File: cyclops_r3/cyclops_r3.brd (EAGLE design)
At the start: 124.5 x 79.9 mm, 107 parts, among them Q1 BC817, Q2 IRF510, U1 MCP4921, U2 MCP4022-50k, U3 317-N, U4 TLV3701, U5 337-N, U6 ADR03, U7 OP1177, U8 LTC2052HV, U9 ZXTD45

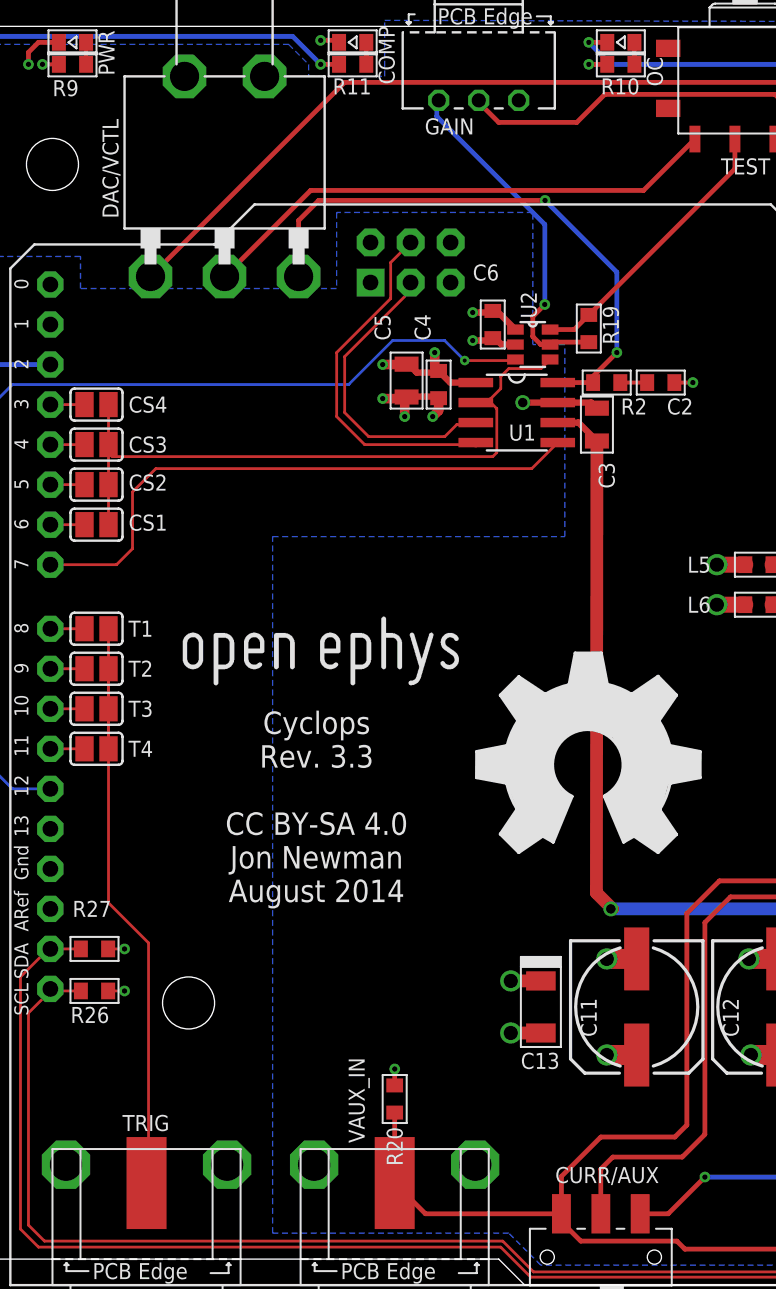
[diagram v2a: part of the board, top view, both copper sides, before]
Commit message: Assembed r3.3 and started a TODO list. Started driver code.
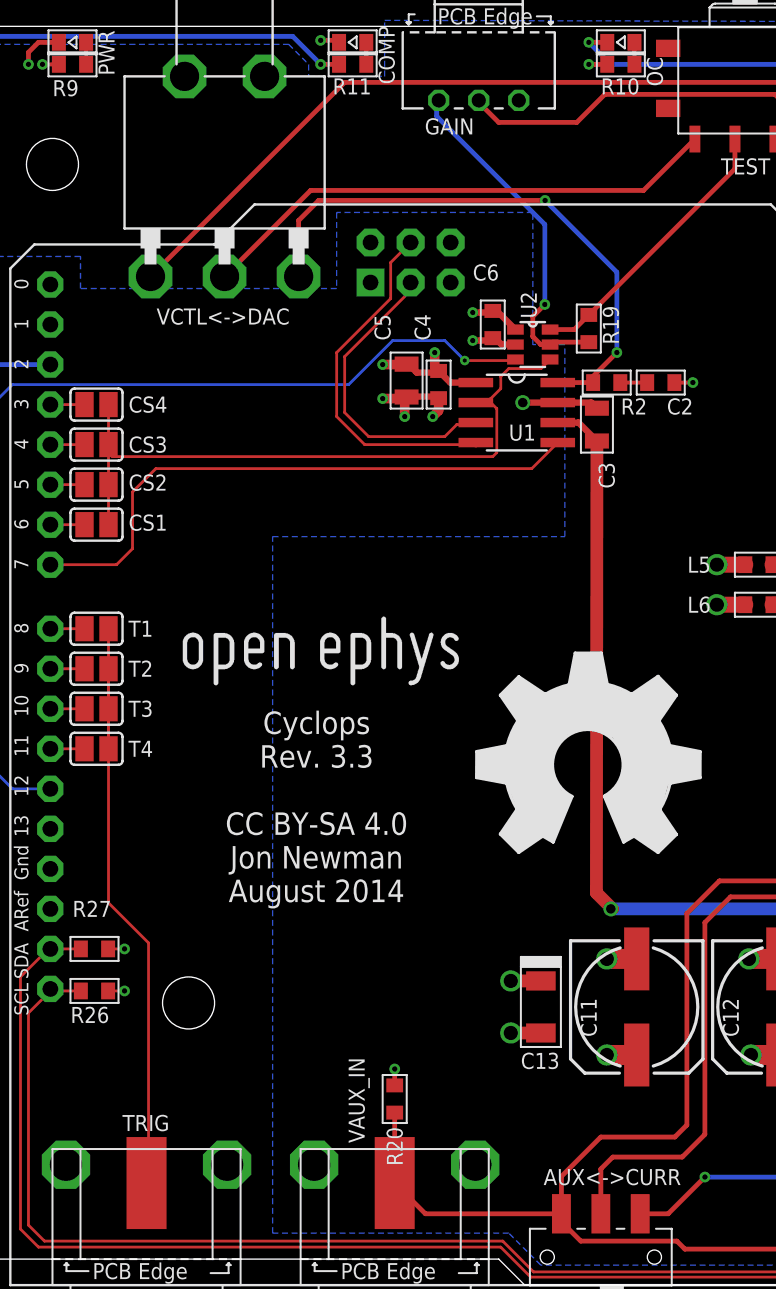
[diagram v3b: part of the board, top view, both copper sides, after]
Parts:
- renumbered CURR/AUX to AUX<->CURR, DAC/VCTL to VCTL<->DAC
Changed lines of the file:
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@@
 <?xml version="1.0" encoding="utf-8"?>
 <!DOCTYPE eagle SYSTEM "eagle.dtd">
-<eagle version="6.5.0">
+<eagle version="6.6.0">
 <drawing>
 <settings>
@@
 <attribute name="VALUE" x="68.714" y="52.705" size="1.016" layer="27" font="vector" ratio="18"/>
 </element>
-<element name="CURR/AUX" library="cyclops" package="JS102011SAQN" value="JS102" x="41.656" y="1.778" smashed="yes">
-<attribute name="NAME" x="45.353" y="7.493" size="1.016" layer="25" font="vector" ratio="18" rot="R180"/>
+<element name="AUX&lt;-&gt;CURR" library="cyclops" package="JS102011SAQN" value="JS102" x="41.656" y="1.778" smashed="yes">
+<attribute name="NAME" x="46.75" y="7.366" size="1.016" layer="25" font="vector" ratio="18" rot="R180"/>
 <attribute name="VALUE" x="43.956" y="2.286" size="1.016" layer="27" font="vector" ratio="18" rot="R180"/>
 </element>
@@
 <attribute name="VALUE" x="35.306" y="73.025" size="1.016" layer="27" font="vector" ratio="18"/>
 </element>
-<element name="DAC/VCTL" library="cyclops" package="2M1-SP1-T2-B4-M6RE" value="2M1" x="17.78" y="76.2" smashed="yes" rot="R270">
-<attribute name="NAME" x="11.049" y="67.691" size="1.016" layer="25" font="vector" ratio="18" rot="R90"/>
+<element name="VCTL&lt;-&gt;DAC" library="cyclops" package="2M1-SP1-T2-B4-M6RE" value="2M1" x="17.78" y="76.2" smashed="yes" rot="R270">
+<attribute name="NAME" x="13.462" y="60.96" size="1.016" layer="25" font="vector" ratio="18"/>
 <attribute name="VALUE" x="16.383" y="73.914" size="1.016" layer="27" font="vector" ratio="18"/>
 </element>
@@
 <signal name="VFB">
 <contactref element="U8" pad="6"/>
-<contactref element="CURR/AUX" pad="2"/>
+<contactref element="AUX&lt;-&gt;CURR" pad="2"/>
 <wire x1="65.084" y1="40.64" x2="60.325" y2="40.64" width="0.3048" layer="1"/>
 <wire x1="60.325" y1="40.64" x2="58.801" y2="39.116" width="0.3048" layer="1"/>
@@
 <contactref element="U1" pad="8"/>
 <contactref element="R2" pad="2"/>
-<contactref element="DAC/VCTL" pad="1"/>
+<contactref element="VCTL&lt;-&gt;DAC" pad="1"/>
 <wire x1="38.1184" y1="68.834" x2="23.749" y2="68.834" width="0.3048" layer="1"/>
 <wire x1="23.749" y1="68.834" x2="22.479" y2="67.564" width="0.3048" layer="1"/>
@@
 <wire x1="60.706" y1="44.069" x2="64.703" y2="44.069" width="0.3048" layer="1"/>
 <wire x1="64.703" y1="44.069" x2="65.084" y2="44.45" width="0.3048" layer="1"/>
-<contactref element="CURR/AUX" pad="1"/>
+<contactref element="AUX&lt;-&gt;CURR" pad="1"/>
 <wire x1="28.575" y1="6.477" x2="30.524" y2="4.528" width="0.3048" layer="1"/>
 <wire x1="30.524" y1="4.528" x2="39.156" y2="4.528" width="0.3048" layer="1"/>
@@
 <signal name="N$34">
 <contactref element="TEST" pad="3"/>
-<contactref element="DAC/VCTL" pad="2"/>
+<contactref element="VCTL&lt;-&gt;DAC" pad="2"/>
 <wire x1="17.78" y1="64.008" x2="23.241" y2="69.469" width="0.3048" layer="1"/>
 <wire x1="23.241" y1="69.469" x2="44.365" y2="69.469" width="0.3048" layer="1"/>
@@
 <signal name="VINPUT">
 <contactref element="VCTL" pad="1"/>
-<contactref element="DAC/VCTL" pad="3"/>
+<contactref element="VCTL&lt;-&gt;DAC" pad="3"/>
 <wire x1="25.4" y1="76.327" x2="65.405" y2="76.327" width="0.3048" layer="1"/>
 <wire x1="65.405" y1="76.327" x2="68.326" y2="73.406" width="0.3048" layer="1"/>
@@
 <wire x1="85.979" y1="8.763" x2="86.487" y2="8.763" width="1.4224" layer="1"/>
 <wire x1="86.487" y1="8.763" x2="87.249" y2="9.525" width="1.4224" layer="1"/>
-<contactref element="CURR/AUX" pad="3"/>
+<contactref element="AUX&lt;-&gt;CURR" pad="3"/>
 <wire x1="44.327" y1="4.699" x2="44.156" y2="4.528" width="0.8128" layer="1" curve="90"/>
 <wire x1="120.269" y1="22.352" x2="120.269" y2="44.323" width="3.048" layer="1"/>

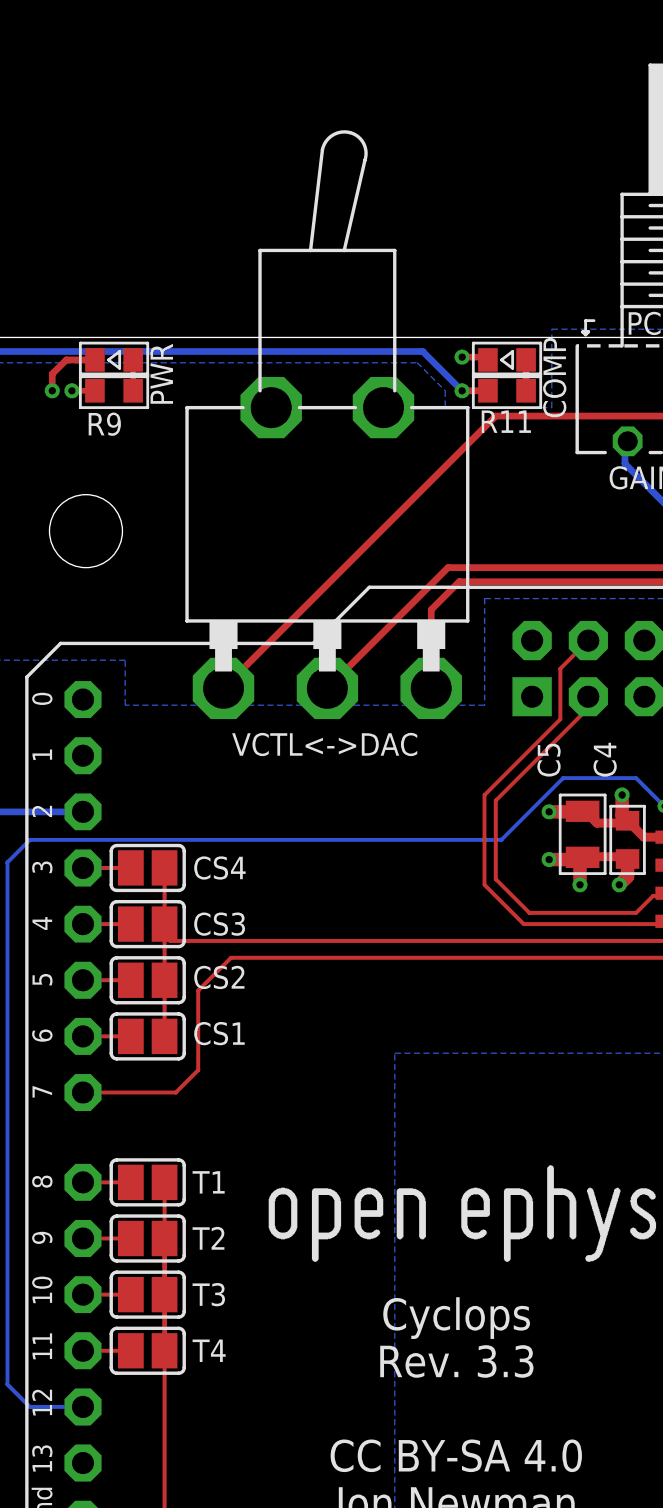
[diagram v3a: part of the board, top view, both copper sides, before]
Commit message: Asthetic fixes to board. Driver has limited functionality and is pretty inefficient, but the base stuff is there.
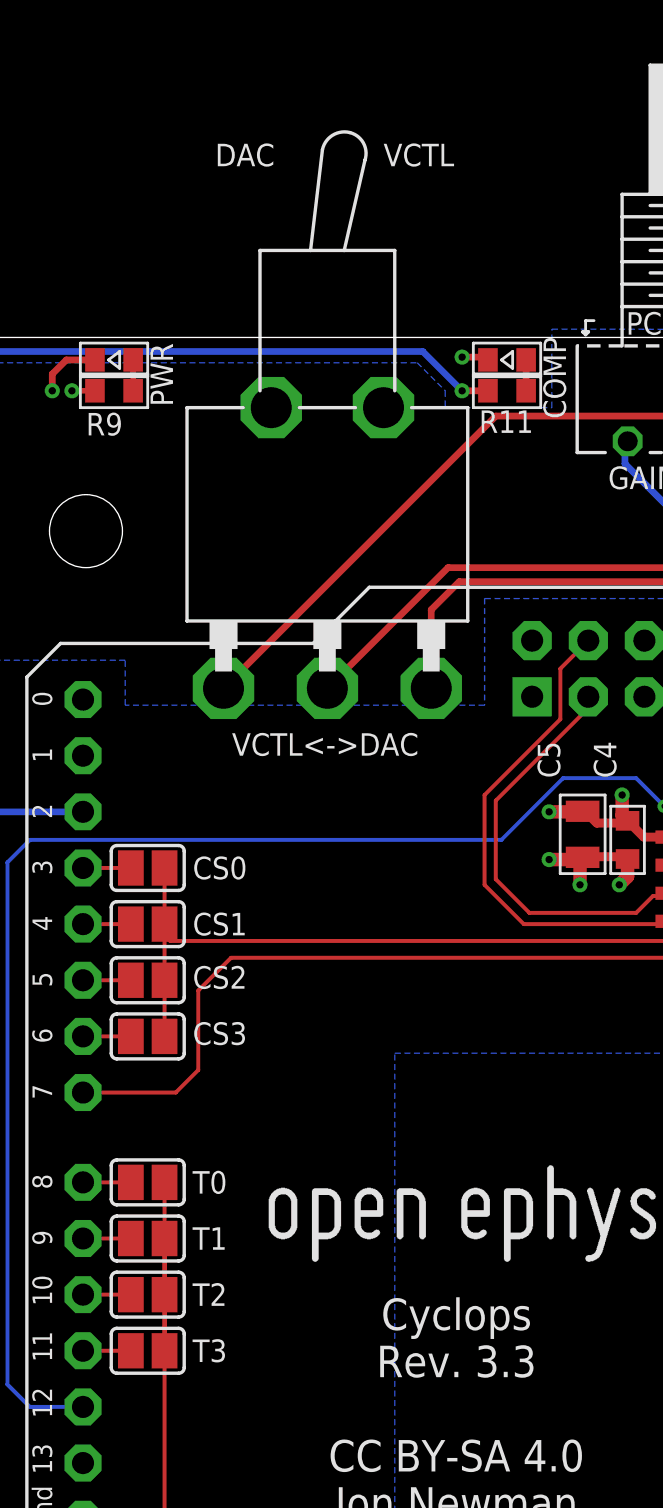
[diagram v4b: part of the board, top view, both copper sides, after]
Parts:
- removed T4: (no value), cyclops:SJ
- added T0: (no value), cyclops:SJ
- moved CS1 5.08 mm to (9.65, 53.3)
- moved CS3 5.08 mm to (9.65, 48.3)
- moved T1 2.54 mm to (9.65, 39.1)
- moved T2 2.54 mm to (9.65, 36.6)
- moved T3 2.54 mm to (9.65, 34.0)
- renumbered CS4 to CS0
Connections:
- net CS1: now also CS1.1; no longer CS3.1
- net CS3: now also CS3.1; no longer CS1.1
- net T0: now also T0.2; no longer T1.2
- net T1: now also T1.2; no longer T2.2
- net T2: now also T2.2; no longer T3.2
- net T3: now also T3.2; no longer T4.2
- net TRIG: now also T0.1; no longer T4.1
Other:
- board text added: "DAC"
- board text added: "VCTL"
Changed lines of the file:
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@@
 <setting verticaltext="up"/>
 </settings>
-<grid distance="0.005" unitdist="inch" unit="inch" style="lines" multiple="1" display="yes" altdistance="0.025" altunitdist="inch" altunit="inch"/>
+<grid distance="0.05" unitdist="inch" unit="inch" style="lines" multiple="1" display="yes" altdistance="0.025" altunitdist="inch" altunit="inch"/>
 <layers>
 <layer number="1" name="Top" color="4" fill="1" visible="yes" active="yes"/>
@@
 <text x="69.215" y="9.525" size="1.016" layer="21" font="vector" ratio="18" rot="R90" align="center">-6V</text>
 <text x="61.595" y="13.97" size="1.016" layer="21" font="vector" ratio="18" align="center">GND</text>
+<text x="20.32" y="87.63" size="1.016" layer="21" font="vector" ratio="18">VCTL</text>
+<text x="12.7" y="87.63" size="1.016" layer="21" font="vector" ratio="18">DAC</text>
 </plain>
 <attributes>
@@
 <attribute name="VALUE" x="72.263" y="45.72" size="1.016" layer="27" font="vector" ratio="18" rot="R90" align="center-left"/>
 </element>
-<element name="CS1" library="cyclops" package="SJ" value="" x="9.652" y="48.26" smashed="yes">
+<element name="CS3" library="cyclops" package="SJ" value="" x="9.652" y="48.26" smashed="yes">
 <attribute name="NAME" x="11.684" y="47.879" size="1.016" layer="25" font="vector" ratio="18"/>
 <attribute name="VALUE" x="10.0521" y="48.26" size="0.02" layer="27"/>
@@
 <attribute name="VALUE" x="10.0521" y="50.8" size="0.02" layer="27"/>
 </element>
-<element name="CS3" library="cyclops" package="SJ" value="" x="9.652" y="53.34" smashed="yes">
+<element name="CS1" library="cyclops" package="SJ" value="" x="9.652" y="53.34" smashed="yes">
 <attribute name="NAME" x="11.684" y="52.832" size="1.016" layer="25" font="vector" ratio="18"/>
 <attribute name="VALUE" x="10.0521" y="53.34" size="0.02" layer="27"/>
 </element>
-<element name="CS4" library="cyclops" package="SJ" value="" x="9.652" y="55.88" smashed="yes">
+<element name="CS0" library="cyclops" package="SJ" value="" x="9.652" y="55.88" smashed="yes">
 <attribute name="NAME" x="11.684" y="55.372" size="1.016" layer="25" font="vector" ratio="18"/>
 <attribute name="VALUE" x="10.0521" y="55.88" size="0.02" layer="27"/>
@@
 <attribute name="VALUE" x="28.575" y="13.589" size="1.016" layer="27" font="vector" ratio="18" rot="R90" align="center-left"/>
 </element>
-<element name="T1" library="cyclops" package="SJ" value="" x="9.652" y="41.656" smashed="yes" rot="R180">
+<element name="T0" library="cyclops" package="SJ" value="" x="9.652" y="41.656" smashed="yes" rot="R180">
 <attribute name="NAME" x="11.684" y="41.148" size="1.016" layer="25" font="vector" ratio="18"/>
 <attribute name="VALUE" x="9.2519" y="41.656" size="0.02" layer="27" rot="R180"/>
 </element>
-<element name="T2" library="cyclops" package="SJ" value="" x="9.652" y="39.116" smashed="yes" rot="R180">
+<element name="T1" library="cyclops" package="SJ" value="" x="9.652" y="39.116" smashed="yes" rot="R180">
 <attribute name="NAME" x="11.684" y="38.608" size="1.016" layer="25" font="vector" ratio="18"/>
 <attribute name="VALUE" x="9.2519" y="39.116" size="0.02" layer="27" rot="R180"/>
 </element>
-<element name="T3" library="cyclops" package="SJ" value="" x="9.652" y="36.576" smashed="yes" rot="R180">
+<element name="T2" library="cyclops" package="SJ" value="" x="9.652" y="36.576" smashed="yes" rot="R180">
 <attribute name="NAME" x="11.684" y="36.068" size="1.016" layer="25" font="vector" ratio="18"/>
 <attribute name="VALUE" x="9.2519" y="36.576" size="0.02" layer="27" rot="R180"/>
 </element>
-<element name="T4" library="cyclops" package="SJ" value="" x="9.652" y="34.036" smashed="yes" rot="R180">
+<element name="T3" library="cyclops" package="SJ" value="" x="9.652" y="34.036" smashed="yes" rot="R180">
 <attribute name="NAME" x="11.684" y="33.528" size="1.016" layer="25" font="vector" ratio="18"/>
 <attribute name="VALUE" x="9.2519" y="34.036" size="0.02" layer="27" rot="R180"/>
@@
 </signal>
 <signal name="CS0">
-<contactref element="CS4" pad="1"/>
+<contactref element="CS0" pad="1"/>
 <contactref element="LEONARDO" pad="D3"/>
 <wire x1="8.89" y1="55.88" x2="6.724" y2="55.88" width="0.1778" layer="1"/>
 </signal>
 <signal name="CS1">
-<contactref element="CS3" pad="1"/>
+<contactref element="CS1" pad="1"/>
 <contactref element="LEONARDO" pad="D4"/>
 <wire x1="6.724" y1="53.34" x2="8.89" y2="53.34" width="0.1778" layer="1"/>
 </signal>
 <signal name="CS3">
-<contactref element="CS1" pad="1"/>
+<contactref element="CS3" pad="1"/>
 <contactref element="LEONARDO" pad="D6"/>
 <wire x1="6.724" y1="48.26" x2="8.89" y2="48.26" width="0.1778" layer="1"/>
@@
 <signal name="CS">
 <contactref element="U1" pad="2"/>
-<contactref element="CS4" pad="2"/>
+<contactref element="CS0" pad="2"/>
+<contactref element="CS1" pad="2"/>
+<contactref element="CS2" pad="2"/>
 <contactref element="CS3" pad="2"/>
-<contactref element="CS2" pad="2"/>
-<contactref element="CS1" pad="2"/>
 <wire x1="10.414" y1="55.88" x2="10.414" y2="53.34" width="0.1778" layer="1"/>
 <wire x1="10.414" y1="52.832" x2="10.414" y2="53.34" width="0.1778" layer="1"/>
@@
 </signal>
 <signal name="TRIG">
+<contactref element="T0" pad="1"/>
 <contactref element="T1" pad="1"/>
 <contactref element="T2" pad="1"/>
 <contactref element="T3" pad="1"/>
-<contactref element="T4" pad="1"/>
 <contactref element="TRIG" pad="1"/>
 <wire x1="12.827" y1="6.477" x2="12.827" y2="9.144" width="0.1778" layer="1"/>
@@
 </signal>
 <signal name="T0">
-<contactref element="T1" pad="2"/>
+<contactref element="T0" pad="2"/>
 <contactref element="LEONARDO" pad="D8"/>
 <wire x1="8.89" y1="41.656" x2="6.724" y2="41.656" width="0.1778" layer="1"/>
 </signal>
 <signal name="T1">
-<contactref element="T2" pad="2"/>
+<contactref element="T1" pad="2"/>
 <contactref element="LEONARDO" pad="D9"/>
 <wire x1="6.724" y1="39.116" x2="8.89" y2="39.116" width="0.1778" layer="1"/>
 </signal>
 <signal name="T2">
-<contactref element="T3" pad="2"/>
+<contactref element="T2" pad="2"/>
 <contactref element="LEONARDO" pad="D10"/>
 <wire x1="8.89" y1="36.576" x2="6.724" y2="36.576" width="0.1778" layer="1"/>
 </signal>
 <signal name="T3">
-<contactref element="T4" pad="2"/>
+<contactref element="T3" pad="2"/>
 <contactref element="LEONARDO" pad="D11"/>
 <wire x1="6.724" y1="34.036" x2="8.89" y2="34.036" width="0.1778" layer="1"/>
